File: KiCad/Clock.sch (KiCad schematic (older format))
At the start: 23 parts, among them SW2 SW_Push, U44 LM555, U45 74LVC1G125, U46 74AHC1G08, U47 74LVC1G32, U48 74LVC1G125

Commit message: Fixed missing grounding on de-bounce cap
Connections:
- net GND: now also C54.2, R60.2
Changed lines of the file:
@@
 	5300 4450 5300 4550
 Wire Wire Line
-	5300 4550 4850 4550
+	5300 4550 5050 4550
 Wire Wire Line
 	4850 4550 4850 4450
@@
 Text Notes 4000 5400 0    50   ~ 0
 Clock derived from 555 timer may be connected to state machine using JP1.\n\nSW2 may be used to manually generate a clock pulse regardless of the position of JP1.
+$Comp
+L power:GND #PWR?
+U 1 1 5E8F5097
+P 5050 4650
+AR Path="/5E359009/5E8F5097" Ref="#PWR?"  Part="1"
+AR Path="/5E356AC1/5E8F5097" Ref="#PWR0233"  Part="1"
+F 0 "#PWR0233" H 5050 4400 50  0001 C CNN
+F 1 "GND" H 5055 4477 50  0000 C CNN
+F 2 "" H 5050 4650 50  0001 C CNN
+F 3 "" H 5050 4650 50  0001 C CNN
+	1    5050 4650
+	1    0    0    -1
+$EndComp
+Wire Wire Line
+	5050 4650 5050 4550
+Connection ~ 5050 4550
+Wire Wire Line
+	5050 4550 4850 4550
 $EndSCHEMATC

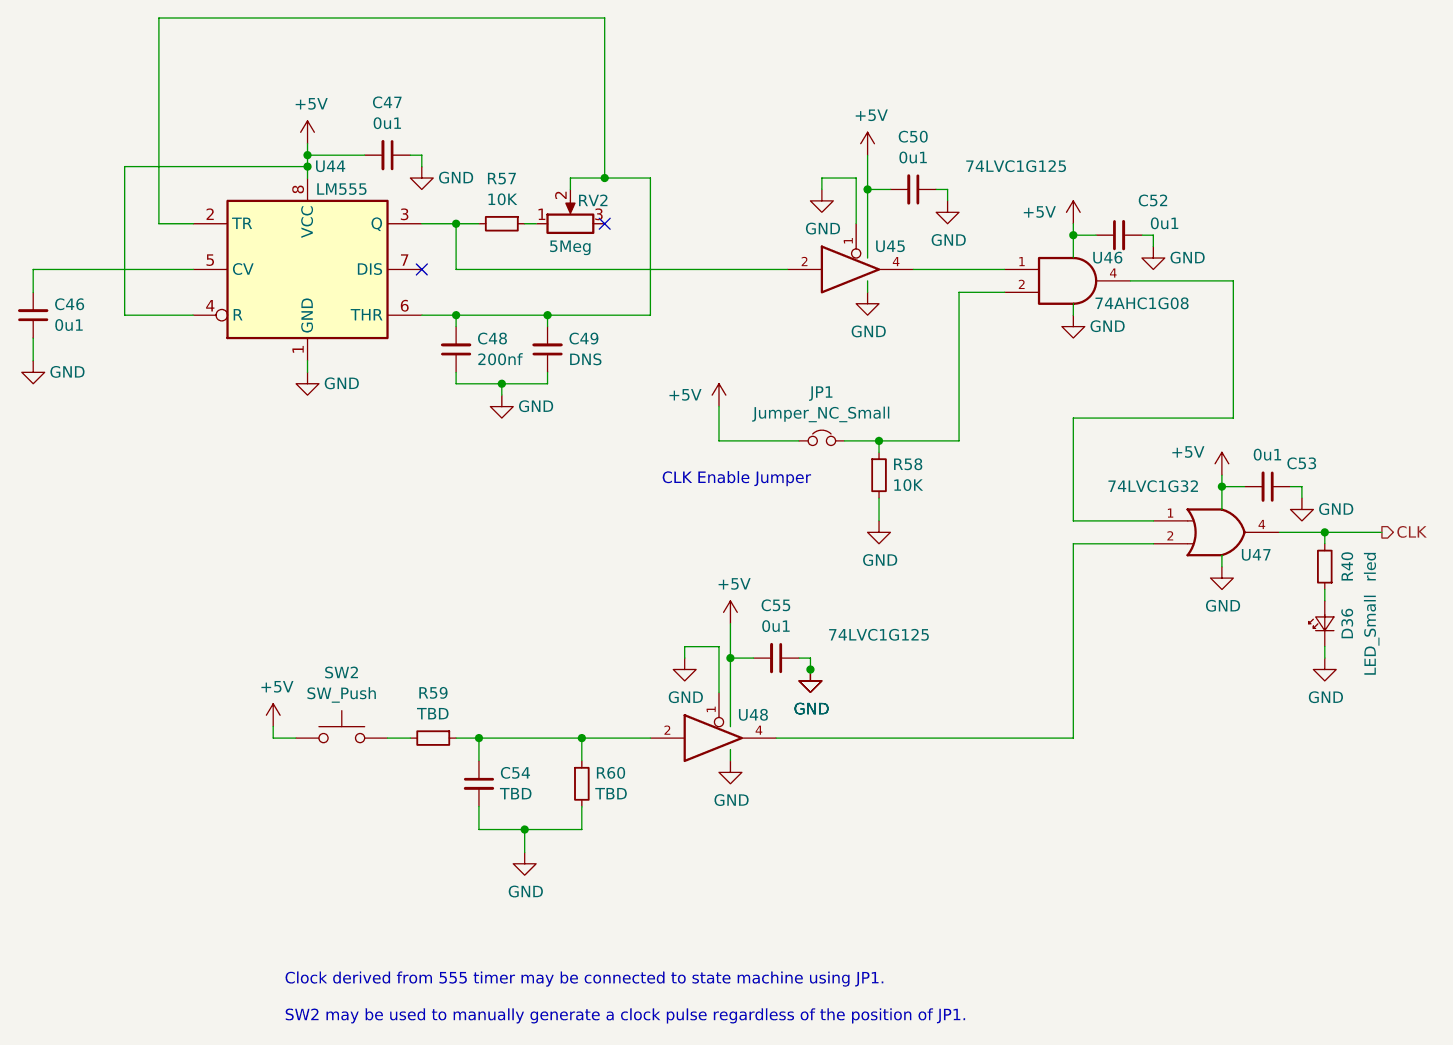
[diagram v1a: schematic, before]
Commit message: Schematic Update First Draft, ERC Passed
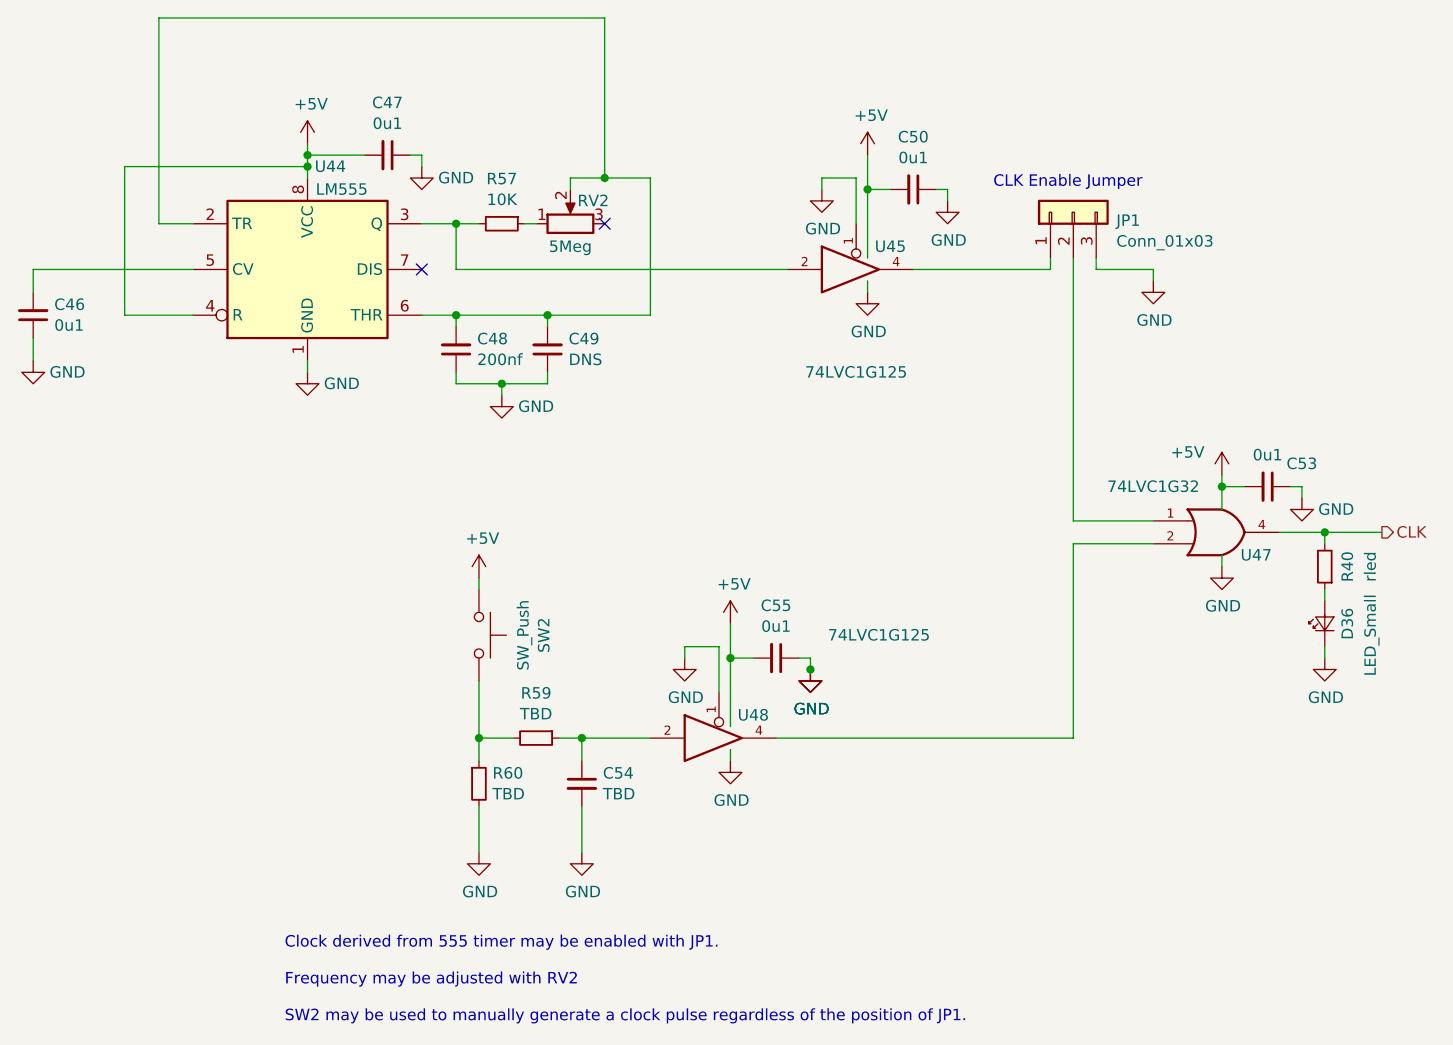
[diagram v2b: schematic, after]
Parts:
- removed C52: 0u1, Capacitor_SMD:C_0603_1608Metric, symbol Device:C_Small
- removed JP1: Jumper_NC_Small, Connector_PinHeader_2.54mm:PinHeader_1x02_P2.54mm_Vertical, symbol Device:Jumper_NC_Small
- removed R58: 10K, Resistor_SMD:R_0603_1608Metric, symbol Device:R_Small
- removed U46: 74AHC1G08, Package_TO_SOT_SMD:SOT-353_SC-70-5, symbol 74xGxx:74AHC1G08
- added JP1: Conn_01x03, Connector_PinHeader_2.54mm:PinHeader_1x03_P2.54mm_Vertical, symbol Connector_Generic:Conn_01x03
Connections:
- net GND: now also JP1.3 (Pin_3)
- net at U47.1: now also JP1.2 (Pin_2)
- net at U45.4: now also JP1.1 (Pin_1)
- net at C54.1, R59.1, U48.2: no longer R60.1
- net at R59.2, SW2.2: now also R60.1
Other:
- note added: "Clock derived from 555 timer may be enabled with JP1.\n\nFrequency may be adjusted with RV2\n\nSW2 may be used to manually generate a clock pulse regardless of the position of JP1."
- note removed: "Clock derived from 555 timer may be connected to state machine using JP1.\n\nSW2 may be used to manually generate a clock pulse regardless of the position of JP1."
- moved on the sheet: C54, R59, R60, SW2

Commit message: First part placement
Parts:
- D36: footprint LED_SMD:LED_0805_2012Metric -> LED_SMD:LED_0603_1608Metric
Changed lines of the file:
@@
 F 0 "D36" H 8550 3550 50  0000 C CNN
 F 1 "LED_Small" H 8500 3450 50  0000 C CNN
-F 2 "LED_SMD:LED_0805_2012Metric" V 8550 3650 50  0001 C CNN
+F 2 "LED_SMD:LED_0603_1608Metric" V 8550 3650 50  0001 C CNN
 F 3 "~" V 8550 3650 50  0001 C CNN
 	1    8550 3650
@@
 P 7800 2150
 AR Path="/5E359009/609DDEB8" Ref="#PWR?"  Part="1"
-AR Path="/5E356AC1/609DDEB8" Ref="#PWR?"  Part="1"
-F 0 "#PWR?" H 7800 1900 50  0001 C CNN
+AR Path="/5E356AC1/609DDEB8" Ref="#PWR0203"  Part="1"
+F 0 "#PWR0203" H 7800 1900 50  0001 C CNN
 F 1 "GND" H 7805 1977 50  0000 C CNN
 F 2 "" H 7800 2150 50  0001 C CNN
@@
 P 4850 4650
 AR Path="/5E359009/60A18C24" Ref="#PWR?"  Part="1"
-AR Path="/5E356AC1/60A18C24" Ref="#PWR?"  Part="1"
-F 0 "#PWR?" H 4850 4400 50  0001 C CNN
+AR Path="/5E356AC1/60A18C24" Ref="#PWR0215"  Part="1"
+F 0 "#PWR0215" H 4850 4400 50  0001 C CNN
 F 1 "GND" H 4855 4477 50  0000 C CNN
 F 2 "" H 4850 4650 50  0001 C CNN

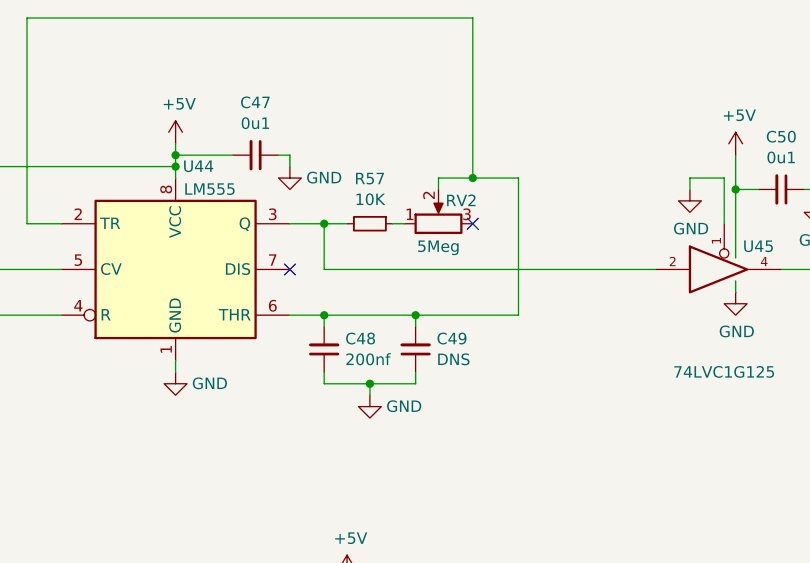
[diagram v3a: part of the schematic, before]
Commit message: Updated Clock Component Values
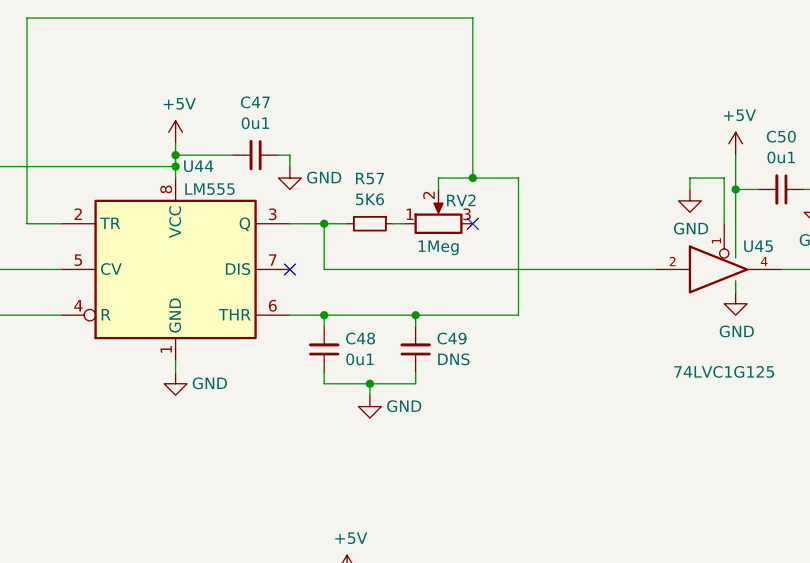
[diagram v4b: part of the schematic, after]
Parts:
- C48: value 200nf -> 0u1
- R57: value 10K -> 5K6
- RV2: value 5Meg -> 1Meg
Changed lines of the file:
@@
 $Descr A4 11693 8268
 encoding utf-8
-Sheet 7 9
+Sheet 6 9
 Title "Schilk_SA-ADC"
 Date "2020-02-03"
@@
 AR Path="/5E356AC1/5EAA82E6" Ref="C48"  Part="1"
 F 0 "C48" H 4658 2404 50  0000 R CNN
-F 1 "200nf" H 4658 2495 50  0000 R CNN
+F 1 "0u1" H 4658 2495 50  0000 R CNN
 F 2 "Capacitor_SMD:C_0603_1608Metric" H 4750 2450 50  0001 C CNN
 F 3 "~" H 4750 2450 50  0001 C CNN
@@
 P 4950 1900
 F 0 "R57" V 4754 1900 50  0000 C CNN
-F 1 "10K" V 4845 1900 50  0000 C CNN
+F 1 "5K6" V 4845 1900 50  0000 C CNN
 F 2 "Resistor_SMD:R_0603_1608Metric" H 4950 1900 50  0001 C CNN
 F 3 "~" H 4950 1900 50  0001 C CNN
@@
 P 5250 1900
 F 0 "RV2" V 5350 1800 50  0000 C CNN
-F 1 "5Meg" V 5150 1900 50  0000 C CNN
+F 1 "1Meg" V 5150 1900 50  0000 C CNN
 F 2 "Potentiometer_THT:Potentiometer_Bourns_3386P_Vertical" H 5250 1900 50  0001 C CNN
 F 3 "~" H 5250 1900 50  0001 C CNN

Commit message: PCB v0.2.
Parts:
- removed JP1: Conn_01x03, Connector_PinHeader_2.54mm:PinHeader_1x03_P2.54mm_Vertical, symbol Connector_Generic:Conn_01x03
- added SW3: SW_Push_SPDT, Connector_PinHeader_2.54mm:PinHeader_1x03_P2.54mm_Vertical, symbol Switch:SW_Push_SPDT
- D36: value LED_Small -> LED
- U44: value LM555 -> NE555DR
- U45, U48: value 74LVC1G125 -> SN74LVC1G125DCK
- U47: value 74LVC1G32 -> SN74LVC1G32DCK
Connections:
- net GND: now also SW3.3 (C)
- net at U47.1: now also SW3.2 (B)
- net at U45.4: now also SW3.1 (A)
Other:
- note removed: "CLK Enable Jumper"
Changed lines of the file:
@@
 AR Path="/5E356AC1/5E45959C" Ref="D36"  Part="1"
 F 0 "D36" H 8550 3550 50  0000 C CNN
-F 1 "LED_Small" H 8500 3450 50  0000 C CNN
+F 1 "LED" H 8500 3450 50  0000 C CNN
 F 2 "LED_SMD:LED_0603_1608Metric" V 8550 3650 50  0001 C CNN
 F 3 "~" V 8550 3650 50  0001 C CNN
@@
 AR Path="/5E356AC1/5EA9E30B" Ref="U45"  Part="1"
 F 0 "U45" H 6650 2200 50  0000 C CNN
-F 1 "74LVC1G125" H 6500 1650 50  0000 C CNN
+F 1 "SN74LVC1G125DCK" H 6500 1650 50  0000 C CNN
 F 2 "Package_TO_SOT_SMD:SOT-353_SC-70-5" H 6500 2100 50  0001 C CNN
 F 3 "http://www.ti.com/lit/sg/scyt129e/scyt129e.pdf" H 6500 2100 50  0001 C CNN
@@
 P 4100 2100
 F 0 "U44" H 4200 2550 50  0000 C CNN
-F 1 "LM555" H 4250 2450 50  0000 C CNN
+F 1 "NE555DR" H 4300 2450 50  0000 C CNN
 F 2 "Package_SO:SOP-8_3.9x4.9mm_P1.27mm" H 4100 2100 50  0001 C CNN
 F 3 "http://www.ti.com/lit/ds/symlink/lm555.pdf" H 4100 2100 50  0001 C CNN
@@
 AR Path="/5E356AC1/5E4D96FB" Ref="U47"  Part="1"
 F 0 "U47" H 8250 3150 50  0000 C CNN
-F 1 "74LVC1G32" H 7800 3450 50  0000 C CNN
+F 1 "SN74LVC1G32DCK" H 8000 2750 50  0000 C CNN
 F 2 "Package_TO_SOT_SMD:SOT-353_SC-70-5" H 8100 3250 50  0001 C CNN
 F 3 "http://www.ti.com/lit/sg/scyt129e/scyt129e.pdf" H 8100 3250 50  0001 C CNN
@@
 AR Path="/5E356AC1/5E549980" Ref="U48"  Part="1"
 F 0 "U48" H 6050 4250 50  0000 C CNN
-F 1 "74LVC1G125" H 6600 4600 50  0000 C CNN
+F 1 "SN74LVC1G125DCK" H 6600 4600 50  0000 C CNN
 F 2 "Package_TO_SOT_SMD:SOT-353_SC-70-5" H 5900 4150 50  0001 C CNN
 F 3 "http://www.ti.com/lit/sg/scyt129e/scyt129e.pdf" H 5900 4150 50  0001 C CNN
@@
 	1    0    0    -1
 $EndComp
-Text Notes 7100 1750 0    50   ~ 0
-CLK Enable Jumper
-$Comp
-L Connector_Generic:Conn_01x03 JP1
-U 1 1 609C6916
-P 7450 1850
-F 0 "JP1" V 7414 1662 50  0000 R CNN
-F 1 "Conn_01x03" V 7323 1662 50  0000 R CNN
-F 2 "Connector_PinHeader_2.54mm:PinHeader_1x03_P2.54mm_Vertical" H 7450 1850 50  0001 C CNN
-F 3 "~" H 7450 1850 50  0001 C CNN
-	1    7450 1850
-	0    -1   -1   0
-$EndComp
-Wire Wire Line
-	7350 2050 7350 2100
 Wire Wire Line
 	6750 2100 7350 2100
 Wire Wire Line
-	7450 2050 7450 3200
-Wire Wire Line
-	7550 2050 7550 2100
-Wire Wire Line
-	7550 2100 7800 2100
-Wire Wire Line
-	7800 2100 7800 2150
+	7550 2250 7600 2250
 $Comp
 L power:GND #PWR?
 U 1 1 609DDEB8
-P 7800 2150
+P 7600 2250
 AR Path="/5E359009/609DDEB8" Ref="#PWR?"  Part="1"
 AR Path="/5E356AC1/609DDEB8" Ref="#PWR0203"  Part="1"
-F 0 "#PWR0203" H 7800 1900 50  0001 C CNN
-F 1 "GND" H 7805 1977 50  0000 C CNN
-F 2 "" H 7800 2150 50  0001 C CNN
-F 3 "" H 7800 2150 50  0001 C CNN
-	1    7800 2150
-	1    0    0    -1
+F 0 "#PWR0203" H 7600 2000 50  0001 C CNN
+F 1 "GND" H 7605 2077 50  0000 C CNN
+F 2 "" H 7600 2250 50  0001 C CNN
+F 3 "" H 7600 2250 50  0001 C CNN
+	1    7600 2250
+	0    -1   -1   0
 $EndComp
 Wire Wire Line
@@
 	4850 3900 4850 4150
 Connection ~ 4850 4150
+$Comp
+L Switch:SW_Push_SPDT SW3
+U 1 1 5F06D594
+P 7450 2500
+F 0 "SW3" V 7496 2312 50  0000 R CNN
+F 1 "SW_Push_SPDT" V 7405 2312 50  0000 R CNN
+F 2 "Connector_PinHeader_2.54mm:PinHeader_1x03_P2.54mm_Vertical" H 7450 2500 50  0001 C CNN
+F 3 "~" H 7450 2500 50  0001 C CNN
+	1    7450 2500
+	0    -1   -1   0
+$EndComp
+Wire Wire Line
+	7450 2700 7450 3200
+Wire Wire Line
+	7550 2250 7550 2300
+Wire Wire Line
+	7350 2100 7350 2300
 $EndSCHEMATC
